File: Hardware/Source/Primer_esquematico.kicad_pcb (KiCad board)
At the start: 2 copper layers, 105 x 24 mm, 6 parts, among them J2 Screw_Terminal_01x06, SW1 SW_Push, U1 XIAO-ESP32-C3-DIP, U3 2472, U4 MICRO SD

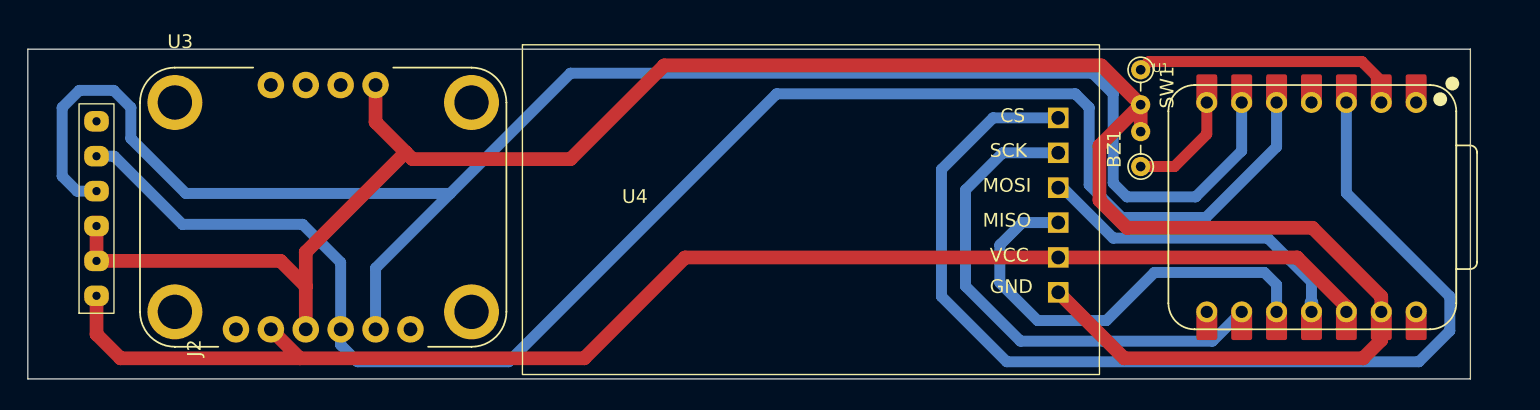
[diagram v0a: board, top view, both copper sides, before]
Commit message: Actualización diseño de PCB
Finalización del diseño de la PCB.
Se completaron los ajustes finales de ruteo, planos de cobre y reglas de fabricación.
Se ejecutó el DRC obteniendo validación completa sin errores ni advertencias críticas.
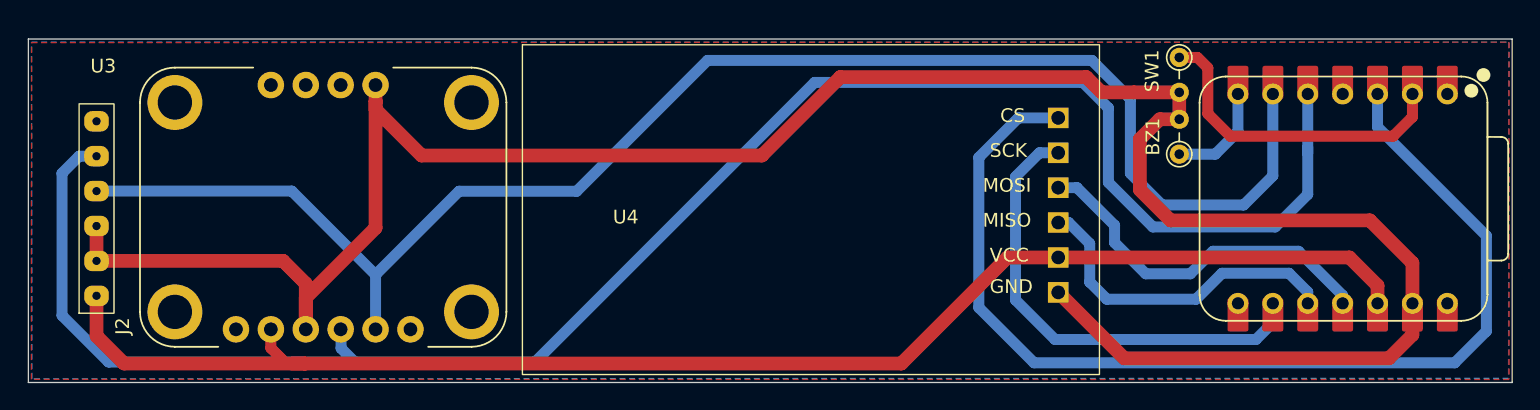
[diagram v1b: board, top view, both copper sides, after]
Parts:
- moved BZ1 2.95 mm to (219.3, 102.1)
- moved SW1 2.95 mm to (219.3, 95.1)
- moved U1 2.35 mm to (231.2, 105.4)
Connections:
- net Net-(BZ1--) renamed GND
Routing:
- net Net-(J2-Pin_5): track 116.1 -> 132.9 mm
- net Net-(J2-Pin_4): track 127.0 -> 112.9 mm
- net GND: track 159.9 -> 169.0 mm
- net Net-(U1-GPIO9_D9_MISO): track 32.8 -> 24.3 mm
- net Net-(U1-GPIO3_A1_D1): track 19.1 -> 23.5 mm
- net Net-(J2-Pin_1): track 103.2 -> 107.6 mm
- net Net-(U1-GPIO8_D8_SCK): track 37.5 -> 34.6 mm
- net Net-(U1-GPIO10_D10_MOSI): track 24.1 -> 26.6 mm
- net Net-(U1-GPIO4_A2_D2): track 78.9 -> 78.0 mm
- added copper zone on B.Cu, net (none)
- added copper zone on F.Cu, net GND
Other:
- board size 105 x 24 mm -> 108 x 25 mm
